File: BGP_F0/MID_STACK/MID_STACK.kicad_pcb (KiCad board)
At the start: 2 copper layers, 0 parts

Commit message: F0 Mid Stack done
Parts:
- added C1: 10n, Capacitors_SMD:C_0805_HandSoldering, F.Cu at (171.0, 108.0)
- added C2: 4.7n, Capacitors_SMD:C_0805_HandSoldering, F.Cu at (178.8, 108.0)
- added P1: CONN_01X04, Connectors_JST:JST_PH_B4B-PH-K_04x2.00mm_Straight, F.Cu at (172.0, 115.0)
- added P2: CONN_01X09, LIBS:Potentiometer_Alpha_Tripple_Vertical_Dual_Shaft, B.Cu at (171.3, 94.0)
- added R1: 12k, Resistors_SMD:R_0603_HandSoldering, F.Cu at (167.0, 104.0)
- added R2: 12k, Resistors_SMD:R_0603_HandSoldering, F.Cu at (183.0, 104.0)
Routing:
- net /MID_I: track 0.00 -> 22.8 mm
- net /MID_O: track 0.00 -> 22.1 mm
- net /F1_1: track 0.00 -> 20.4 mm
- net /VOL2: track 0.00 -> 15.2 mm, vias 0 -> 1
- net /F1_2: track 0.00 -> 14.5 mm
- net /F2_2: track 0.00 -> 8.46 mm
- net Net-(C1-Pad2): track 0.00 -> 5.06 mm
- added copper zone on F.Cu, net /Vref
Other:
- board outline added: 20 x 26 mm

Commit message: Removed old boards, all F0 are now 26mm deep
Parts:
- moved C1 2.00 mm to (171.0, 110.0)
- moved C2 2.00 mm to (178.8, 110.0)
- moved P2 2.00 mm to (171.3, 96.0)
- moved R1 2.00 mm to (167.0, 106.0)
- moved R2 2.00 mm to (183.0, 106.0), turned to 270 degrees
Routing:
- net /F1_1: track 20.4 -> 15.0 mm
- net /MID_O: track 22.1 -> 20.1 mm
- net /MID_I: track 22.8 -> 20.9 mm
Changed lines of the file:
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@@
   (general
     (links 13)
-    (no_connects 0)
-    (area 164.924999 91.924999 185.075001 118.075001)
+    (no_connects 1)
+    (area 164.924999 88.649999 185.755 119.655)
     (thickness 1.6)
     (drawings 8)
@@
   )
   (module LIBS:Potentiometer_Alpha_Tripple_Vertical_Dual_Shaft (layer B.Cu)
-    (at 171.35 94 90)
+    (at 171.35 96 90)
     (descr "Potentiometer, vertically mounted, Omeg PC16PU, Omeg PC16PU, Omeg PC16PU, Vishay/Spectrol 248GJ/249GJ Single, Vishay/Spectrol 248GJ/249GJ Single, Vishay/Spectrol 248GJ/249GJ Single, Vishay/Spectrol 248GH/249GH Single, Vishay/Spectrol 148/149 Single, Vishay/Spectrol 148/149 Single, Vishay/Spectrol 148/149 Single, Vishay/Spectrol 148A/149A Single with mounting plates, Vishay/Spectrol 148/149 Double, Vishay/Spectrol 148A/149A Double with mounting plates, Piher PC-16 Single, Piher PC-16 Single, Piher PC-16 Single, Piher PC-16SV Single, Piher PC-16 Double, Piher PC-16 Triple, Piher T16H Single, Piher T16L Single, Piher T16H Double, Alps RK163 Single, Alps RK163 Double, Alps RK097 Single, Alps RK097 Double, http://www.alps.com/prod/info/E/HTML/Potentiometer/RotaryPotentiometers/RK097/RK09712100AV.html")
     (tags "Potentiometer vertical  Omeg PC16PU  Omeg PC16PU  Omeg PC16PU  Vishay/Spectrol 248GJ/249GJ Single  Vishay/Spectrol 248GJ/249GJ Single  Vishay/Spectrol 248GJ/249GJ Single  Vishay/Spectrol 248GH/249GH Single  Vishay/Spectrol 148/149 Single  Vishay/Spectrol 148/149 Single  Vishay/Spectrol 148/149 Single  Vishay/Spectrol 148A/149A Single with mounting plates  Vishay/Spectrol 148/149 Double  Vishay/Spectrol 148A/149A Double with mounting plates  Piher PC-16 Single  Piher PC-16 Single  Piher PC-16 Single  Piher PC-16SV Single  Piher PC-16 Double  Piher PC-16 Triple  Piher T16H Single  Piher T16L Single  Piher T16H Double  Alps RK163 Single  Alps RK163 Double  Alps RK097 Single  Alps RK097 Double Dual Shaft")
@@
   )
   (module Capacitors_SMD:C_0805_HandSoldering (layer F.Cu)
-    (at 171 108 180)
+    (at 171 110 180)
     (descr "Capacitor SMD 0805, hand soldering")
     (tags "capacitor 0805")
@@
   )
   (module Capacitors_SMD:C_0805_HandSoldering (layer F.Cu)
-    (at 178.75 108)
+    (at 178.75 110)
     (descr "Capacitor SMD 0805, hand soldering")
     (tags "capacitor 0805")
@@
   )
   (module Resistors_SMD:R_0603_HandSoldering (layer F.Cu)
-    (at 167 104 90)
+    (at 167 106 90)
     (descr "Resistor SMD 0603, hand soldering")
     (tags "resistor 0603")
@@
   )
   (module Resistors_SMD:R_0603_HandSoldering (layer F.Cu)
-    (at 183 104 90)
+    (at 183 106 270)
     (descr "Resistor SMD 0603, hand soldering")
     (tags "resistor 0603")
     (attr smd)
-    (fp_text reference R2 (at -1.3 -1.2 90) (layer F.SilkS)
-      (effects (font (size 0.6 0.6) (thickness 0.15)))
-    )
-    (fp_text value 12k (at 0 1.9 90) (layer F.Fab) hide
+    (fp_text reference R2 (at -1.3 -1.2 270) (layer F.SilkS)
+      (effects (font (size 0.6 0.6) (thickness 0.15)))
+    )
+    (fp_text value 12k (at 0 1.9 270) (layer F.Fab) hide
       (effects (font (size 0.6 0.6) (thickness 0.15)))
     )
@@
     (fp_line (start 0.5 0.675) (end -0.5 0.675) (layer F.SilkS) (width 0.15))
     (fp_line (start -0.5 -0.675) (end 0.5 -0.675) (layer F.SilkS) (width 0.15))
-    (pad 1 smd rect (at -1.1 0 90) (size 1.2 0.9) (layers F.Cu F.Paste F.Mask)
+    (pad 1 smd rect (at -1.1 0 270) (size 1.2 0.9) (layers F.Cu F.Paste F.Mask)
       (net 8 /F2_2))
-    (pad 2 smd rect (at 1.1 0 90) (size 1.2 0.9) (layers F.Cu F.Paste F.Mask)
+    (pad 2 smd rect (at 1.1 0 270) (size 1.2 0.9) (layers F.Cu F.Paste F.Mask)
       (net 4 /Vref))
     (model Resistors_SMD.3dshapes/R_0603_HandSoldering.wrl
@@
   (gr_line (start 165 92) (end 165 118) (layer Edge.Cuts) (width 0.15))
   (gr_line (start 185 92) (end 165 92) (layer Edge.Cuts) (width 0.15))
-  (segment (start 172.2 106.5) (end 172.2 106.075736) (width 0.4) (layer B.Cu) (net 1))
-  (segment (start 173 105.275736) (end 173 96) (width 0.4) (layer B.Cu) (net 1))
-  (segment (start 173 96) (end 174.100001 94.899999) (width 0.4) (layer B.Cu) (net 1))
-  (segment (start 172.2 106.075736) (end 173 105.275736) (width 0.4) (layer B.Cu) (net 1))
-  (segment (start 174.100001 94.899999) (end 175 94) (width 0.4) (layer B.Cu) (net 1))
-  (segment (start 172.25 108) (end 172.25 106.55) (width 0.4) (layer F.Cu) (net 1))
-  (segment (start 172.25 106.55) (end 172.2 106.5) (width 0.4) (layer F.Cu) (net 1))
-  (via (at 172.2 106.5) (size 0.6) (drill 0.4) (layers F.Cu B.Cu) (net 1))
-  (segment (start 167 105.1) (end 167 107) (width 0.4) (layer F.Cu) (net 2))
-  (segment (start 167 107) (end 168 108) (width 0.4) (layer F.Cu) (net 2))
-  (segment (start 168 108) (end 169.75 108) (width 0.4) (layer F.Cu) (net 2))
-  (segment (start 171.35 104) (end 171.35 102.727208) (width 0.4) (layer B.Cu) (net 3))
-  (segment (start 171.35 102.727208) (end 171.35 99) (width 0.4) (layer B.Cu) (net 3))
+  (segment (start 172.2 108.5) (end 172.2 108.075736) (width 0.4) (layer B.Cu) (net 1))
+  (segment (start 173 107.275736) (end 173 98) (width 0.4) (layer B.Cu) (net 1))
+  (segment (start 173 98) (end 174.100001 96.899999) (width 0.4) (layer B.Cu) (net 1))
+  (segment (start 172.2 108.075736) (end 173 107.275736) (width 0.4) (layer B.Cu) (net 1))
+  (segment (start 174.100001 96.899999) (end 175 96) (width 0.4) (layer B.Cu) (net 1))
+  (segment (start 172.25 110) (end 172.25 108.55) (width 0.4) (layer F.Cu) (net 1))
+  (segment (start 172.25 108.55) (end 172.2 108.5) (width 0.4) (layer F.Cu) (net 1))
+  (via (at 172.2 108.5) (size 0.6) (drill 0.4) (layers F.Cu B.Cu) (net 1))
+  (segment (start 167 107.1) (end 167 109) (width 0.4) (layer F.Cu) (net 2))
+  (segment (start 167 109) (end 168 110) (width 0.4) (layer F.Cu) (net 2))
+  (segment (start 168 110) (end 169.75 110) (width 0.4) (layer F.Cu) (net 2))
+  (segment (start 171.35 106) (end 171.35 104.727208) (width 0.4) (layer B.Cu) (net 3))
+  (segment (start 171.35 104.727208) (end 171.35 101) (width 0.4) (layer B.Cu) (net 3))
   (segment (start 174 115) (end 174 114.75) (width 0.4) (layer F.Cu) (net 3))
   (segment (start 174 114.75) (end 175.35 113.4) (width 0.4) (layer F.Cu) (net 3))
-  (segment (start 175.35 113.4) (end 175.35 108) (width 0.4) (layer F.Cu) (net 3))
-  (segment (start 177.5 108) (end 175.35 108) (width 0.4) (layer F.Cu) (net 3))
-  (segment (start 175.35 108) (end 171.35 104) (width 0.4) (layer F.Cu) (net 3))
+  (segment (start 177.5 110) (end 175.35 110) (width 0.4) (layer F.Cu) (net 3))
+  (segment (start 175.35 110) (end 171.35 106) (width 0.4) (layer F.Cu) (net 3))
   (segment (start 178 114.75) (end 178 115) (width 0.4) (layer B.Cu) (net 4))
-  (segment (start 171.35 94) (end 171.35 95.272792) (width 0.4) (layer B.Cu) (net 5))
-  (segment (start 169.5 97.122792) (end 169.5 111.25) (width 0.4) (layer B.Cu) (net 5))
-  (segment (start 171.35 95.272792) (end 169.5 97.122792) (width 0.4) (layer B.Cu) (net 5))
-  (segment (start 169.5 111.25) (end 172 113.75) (width 0.4) (layer B.Cu) (net 5))
+  (segment (start 171.85 113.75) (end 169.5 111.4) (width 0.4) (layer B.Cu) (net 5))
+  (segment (start 169.5 111.4) (end 169.5 99.122792) (width 0.4) (layer B.Cu) (net 5))
+  (segment (start 172 113.75) (end 171.85 113.75) (width 0.4) (layer B.Cu) (net 5))
+  (segment (start 171.35 96) (end 171.35 97.272792) (width 0.4) (layer B.Cu) (net 5))
+  (segment (start 171.35 97.272792) (end 169.5 99.122792) (width 0.4) (layer B.Cu) (net 5))
   (segment (start 172 113.75) (end 172 115) (width 0.4) (layer B.Cu) (net 5))
-  (segment (start 178.65 94) (end 178.65 95.272792) (width 0.4) (layer B.Cu) (net 6))
-  (segment (start 178.65 95.272792) (end 177 96.922792) (width 0.4) (layer B.Cu) (net 6))
-  (segment (start 177 96.922792) (end 177 112.75) (width 0.4) (layer B.Cu) (net 6))
+  (segment (start 177 112.75) (end 177 98.922792) (width 0.4) (layer B.Cu) (net 6))
+  (segment (start 178.65 96) (end 178.65 97.272792) (width 0.4) (layer B.Cu) (net 6))
+  (segment (start 178.65 97.272792) (end 177 98.922792) (width 0.4) (layer B.Cu) (net 6))
   (segment (start 177 112.75) (end 176 113.75) (width 0.4) (layer B.Cu) (net 6))
   (segment (start 176 113.75) (end 176 115) (width 0.4) (layer B.Cu) (net 6))
-  (segment (start 167 102.9) (end 167 102) (width 0.4) (layer F.Cu) (net 7))
-  (segment (start 167 102) (end 168 101) (width 0.4) (layer F.Cu) (net 7))
-  (segment (start 168 101) (end 174.2 101) (width 0.4) (layer F.Cu) (net 7))
-  (segment (start 174.2 101) (end 175 100.2) (width 0.4) (layer F.Cu) (net 7))
-  (segment (start 175 100.2) (end 175 99) (width 0.4) (layer F.Cu) (net 7))
-  (segment (start 175 99) (end 178.65 99) (width 0.4) (layer F.Cu) (net 7))
-  (segment (start 178.65 104) (end 179.75 105.1) (width 0.4) (layer F.Cu) (net 8))
-  (segment (start 179.75 105.1) (end 183 105.1) (width 0.4) (layer F.Cu) (net 8))
-  (segment (start 175 104) (end 178.65 104) (width 0.4) (layer F.Cu) (net 8))
+  (segment (start 167 104.9) (end 167 104) (width 0.4) (layer F.Cu) (net 7))
+  (segment (start 167 104) (end 168 103) (width 0.4) (layer F.Cu) (net 7))
+  (segment (start 168 103) (end 174.2 103) (width 0.4) (layer F.Cu) (net 7))
+  (segment (start 174.2 103) (end 175 102.2) (width 0.4) (layer F.Cu) (net 7))
+  (segment (start 175 102.2) (end 175 101) (width 0.4) (layer F.Cu) (net 7))
+  (segment (start 175 101) (end 178.65 101) (width 0.4) (layer F.Cu) (net 7))
+  (segment (start 183 104.9) (end 179.75 104.9) (width 0.4) (layer F.Cu) (net 8))
+  (segment (start 179.75 104.9) (end 178.65 106) (width 0.4) (layer F.Cu) (net 8))
+  (segment (start 175 106) (end 178.65 106) (width 0.4) (layer F.Cu) (net 8))
   (zone (net 4) (net_name /Vref) (layer F.Cu) (hatch edge 0.508)
     (connect_pads (clearance 0.3))

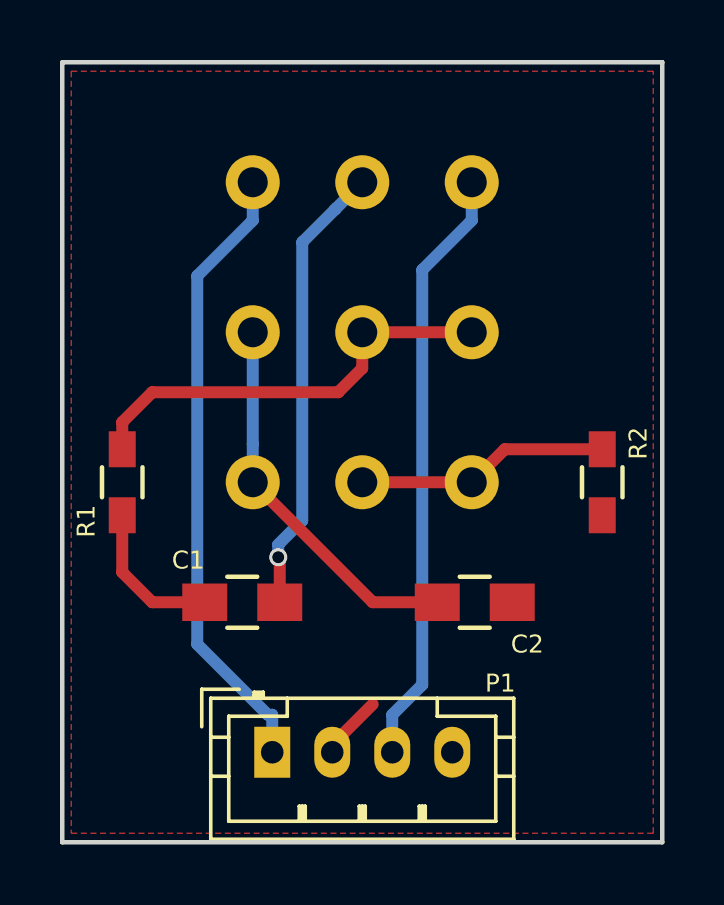
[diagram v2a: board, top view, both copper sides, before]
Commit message: BT and MID pot gain ctrl reversed for proper action
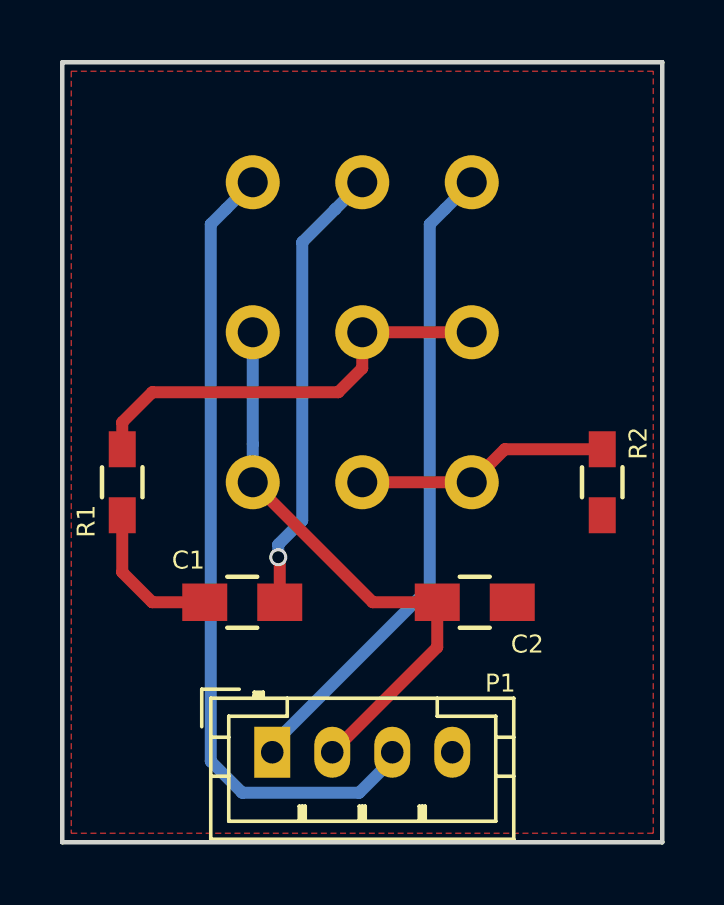
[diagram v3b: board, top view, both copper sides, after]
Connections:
- P2 pad 1: /MID_I -> /MID_O
- P2 pad 3: /MID_O -> /MID_I
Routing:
- net /MID_O: track 20.1 -> 27.1 mm
- net /F1_1: track 15.0 -> 19.3 mm
- net /MID_I: track 20.9 -> 21.8 mm
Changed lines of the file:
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@@
   (general
     (links 13)
-    (no_connects 1)
-    (area 164.924999 88.649999 185.755 119.655)
+    (no_connects 0)
+    (area 164.924999 91.924999 185.075001 118.075001)
     (thickness 1.6)
     (drawings 8)
-    (tracks 38)
+    (tracks 39)
     (zones 0)
     (modules 6)
@@
     (fp_line (start 2.15 10.6) (end -15.15 10.6) (layer B.CrtYd) (width 0.05))
     (pad 3 thru_hole circle (at 0 7.3 90) (size 1.8 1.8) (drill 1) (layers *.Cu *.Mask)
-      (net 6 /MID_O))
+      (net 5 /MID_I))
     (pad 2 thru_hole circle (at 0 3.65 90) (size 1.8 1.8) (drill 1) (layers *.Cu *.Mask)
       (net 1 /VOL2))
     (pad 1 thru_hole circle (at 0 0 90) (size 1.8 1.8) (drill 1) (layers *.Cu *.Mask)
-      (net 5 /MID_I))
+      (net 6 /MID_O))
     (pad 6 thru_hole circle (at -5 7.3 90) (size 1.8 1.8) (drill 1) (layers *.Cu *.Mask)
       (net 7 /F1_2))
@@
   (segment (start 167 109) (end 168 110) (width 0.4) (layer F.Cu) (net 2))
   (segment (start 168 110) (end 169.75 110) (width 0.4) (layer F.Cu) (net 2))
+  (segment (start 174 115) (end 177.5 111.5) (width 0.4) (layer F.Cu) (net 3))
+  (segment (start 177.5 111.5) (end 177.5 110) (width 0.4) (layer F.Cu) (net 3))
   (segment (start 171.35 106) (end 171.35 104.727208) (width 0.4) (layer B.Cu) (net 3))
   (segment (start 171.35 104.727208) (end 171.35 101) (width 0.4) (layer B.Cu) (net 3))
-  (segment (start 174 115) (end 174 114.75) (width 0.4) (layer F.Cu) (net 3))
-  (segment (start 174 114.75) (end 175.35 113.4) (width 0.4) (layer F.Cu) (net 3))
   (segment (start 177.5 110) (end 175.35 110) (width 0.4) (layer F.Cu) (net 3))
   (segment (start 175.35 110) (end 171.35 106) (width 0.4) (layer F.Cu) (net 3))
   (segment (start 178 114.75) (end 178 115) (width 0.4) (layer B.Cu) (net 4))
-  (segment (start 171.85 113.75) (end 169.5 111.4) (width 0.4) (layer B.Cu) (net 5))
-  (segment (start 169.5 111.4) (end 169.5 99.122792) (width 0.4) (layer B.Cu) (net 5))
-  (segment (start 172 113.75) (end 171.85 113.75) (width 0.4) (layer B.Cu) (net 5))
-  (segment (start 171.35 96) (end 171.35 97.272792) (width 0.4) (layer B.Cu) (net 5))
-  (segment (start 171.35 97.272792) (end 169.5 99.122792) (width 0.4) (layer B.Cu) (net 5))
-  (segment (start 172 113.75) (end 172 115) (width 0.4) (layer B.Cu) (net 5))
-  (segment (start 177 112.75) (end 177 98.922792) (width 0.4) (layer B.Cu) (net 6))
-  (segment (start 178.65 96) (end 178.65 97.272792) (width 0.4) (layer B.Cu) (net 6))
-  (segment (start 178.65 97.272792) (end 177 98.922792) (width 0.4) (layer B.Cu) (net 6))
-  (segment (start 177 112.75) (end 176 113.75) (width 0.4) (layer B.Cu) (net 6))
-  (segment (start 176 113.75) (end 176 115) (width 0.4) (layer B.Cu) (net 6))
+  (segment (start 172 115) (end 172 114.75) (width 0.4) (layer B.Cu) (net 5))
+  (segment (start 172 114.75) (end 177.249999 109.500001) (width 0.4) (layer B.Cu) (net 5))
+  (segment (start 177.249999 109.500001) (end 177.249999 97.400001) (width 0.4) (layer B.Cu) (net 5))
+  (segment (start 177.750001 96.899999) (end 178.65 96) (width 0.4) (layer B.Cu) (net 5))
+  (segment (start 177.249999 97.400001) (end 177.750001 96.899999) (width 0.4) (layer B.Cu) (net 5))
+  (segment (start 176 115) (end 176 115.25) (width 0.4) (layer B.Cu) (net 6))
+  (segment (start 176 115.25) (end 174.899999 116.350001) (width 0.4) (layer B.Cu) (net 6))
+  (segment (start 174.899999 116.350001) (end 170.999999 116.350001) (width 0.4) (layer B.Cu) (net 6))
+  (segment (start 170.999999 116.350001) (end 169.949999 115.300001) (width 0.4) (layer B.Cu) (net 6))
+  (segment (start 169.949999 115.300001) (end 169.949999 97.400001) (width 0.4) (layer B.Cu) (net 6))
+  (segment (start 169.949999 97.400001) (end 170.450001 96.899999) (width 0.4) (layer B.Cu) (net 6))
+  (segment (start 170.450001 96.899999) (end 171.35 96) (width 0.4) (layer B.Cu) (net 6))
   (segment (start 167 104.9) (end 167 104) (width 0.4) (layer F.Cu) (net 7))
   (segment (start 167 104) (end 168 103) (width 0.4) (layer F.Cu) (net 7))

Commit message: Some Changes
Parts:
- moved P2 0.10 mm to (171.2, 96.0)

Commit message: Mid Buff
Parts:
- R1, R2: value 12k -> 6.8k
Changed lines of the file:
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@@
-(kicad_pcb (version 4) (host pcbnew 4.0.4-1.fc24-product)
+(kicad_pcb (version 4) (host pcbnew 4.0.7)
   (general
     (links 13)
@@
       (effects (font (size 0.6 0.6) (thickness 0.15)))
     )
-    (fp_text value 12k (at 0 1.9 90) (layer F.Fab) hide
+    (fp_text value 6.8k (at 0 1.9 90) (layer F.Fab) hide
       (effects (font (size 0.6 0.6) (thickness 0.15)))
     )
@@
       (effects (font (size 0.6 0.6) (thickness 0.15)))
     )
-    (fp_text value 12k (at 0 1.9 270) (layer F.Fab) hide
-      (effects (font (size 0.6 0.6) (thickness 0.15)))
-    )
+    (fp_text value 6.8k (at 0 1.9 270) (layer F.Fab) hide
+      (effects (font (size 0.6 0.6) (thickness 0.15)))
+    )

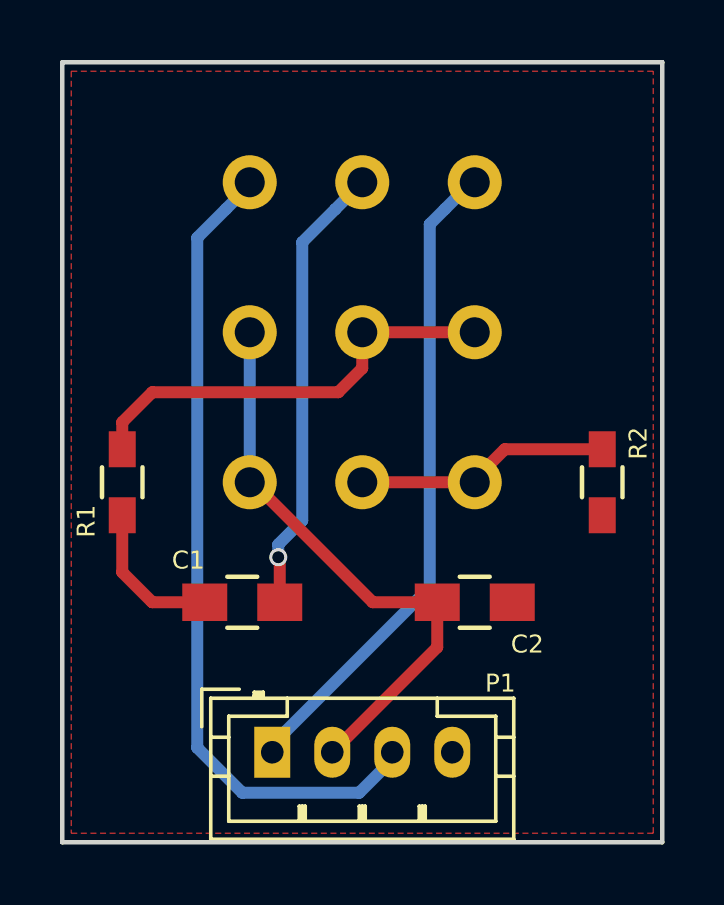
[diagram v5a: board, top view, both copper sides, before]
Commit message: Change some caps to TH, updated BOM - need to recreate
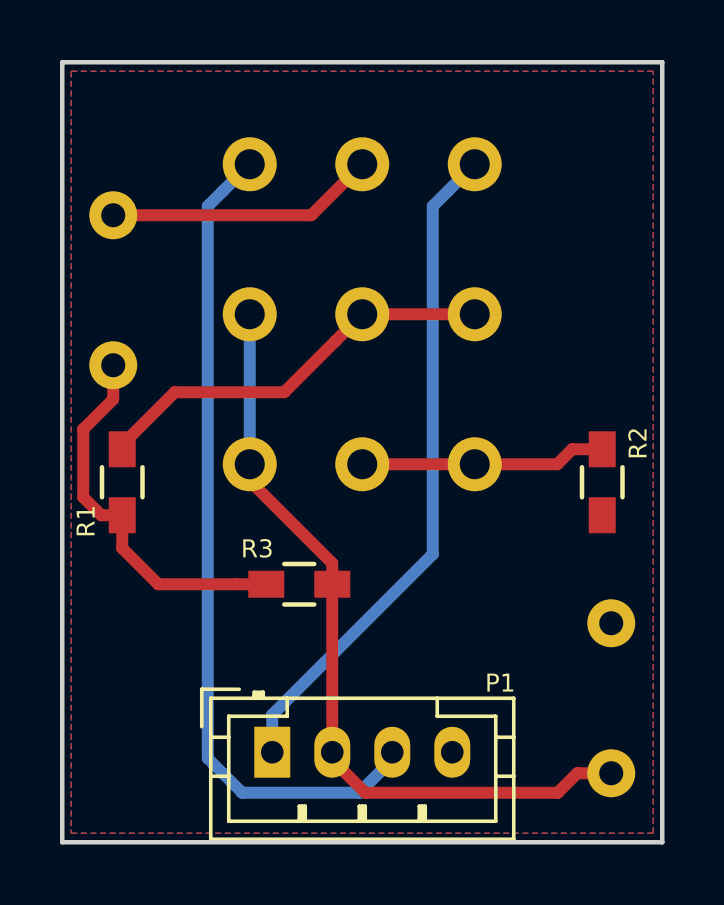
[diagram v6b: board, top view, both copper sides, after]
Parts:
- added R3: 100k, Resistors_SMD:R_0603_HandSoldering, F.Cu at (172.9, 109.4)
- C1: value 10n -> 22n; footprint Capacitors_SMD:C_0805_HandSoldering -> Capacitor_THT:C_Rect_L7.2mm_W2.5mm_P5.00mm_FKS2_FKP2_MKS2_MKP2; moved to B.Cu
- C2: value 4.7n -> 10n; footprint Capacitors_SMD:C_0805_HandSoldering -> Capacitor_THT:C_Rect_L7.2mm_W2.5mm_P5.00mm_FKS2_FKP2_MKS2_MKP2; moved to B.Cu
- R1, R2: value 6.8k -> 4.7k
- moved C1 13.6 mm to (166.7, 97.1), turned to 270 degrees
- moved C2 7.29 mm to (183.3, 115.7), turned to 90 degrees
- moved P2 0.60 mm to (171.2, 95.4)
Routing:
- net Net-(C1-Pad2): track 5.06 -> 12.8 mm
- net /F1_1: track 19.3 -> 25.5 mm
- net /VOL2: track 15.2 -> 9.00 mm, vias 1 -> 0
- net /MID_I: track 21.8 -> 22.6 mm
- net /F1_2: track 14.5 -> 13.7 mm
- added copper zone on B.Cu, net (none)
